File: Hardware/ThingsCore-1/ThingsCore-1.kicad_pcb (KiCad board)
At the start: 6 copper layers, 30 x 51 mm, 8 parts, among them U2 K4B4G1646E-BYMA, U6 LAN8742A, U7 STM32MP133DAE7, U8 W25Q256JVEIQ, U9 TF-PUSH

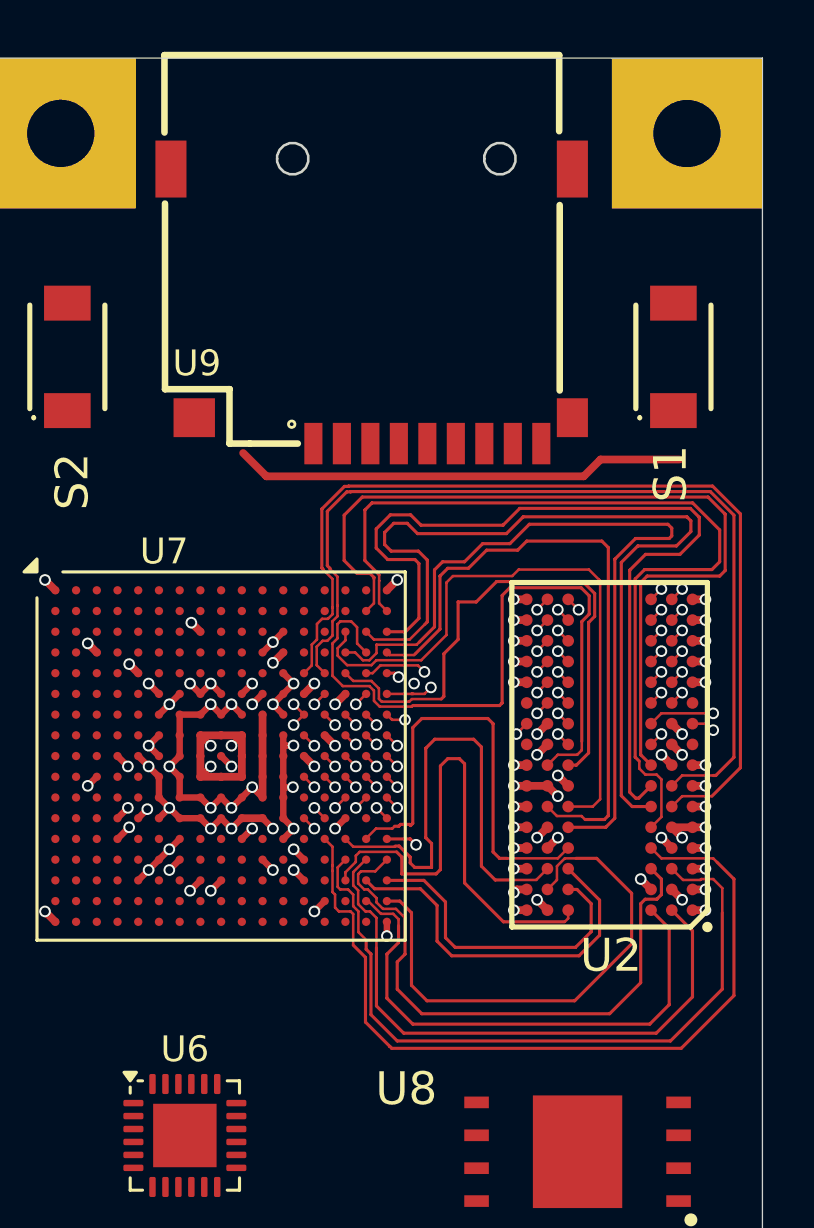
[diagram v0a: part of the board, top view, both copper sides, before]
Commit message: rules and ddr3 reroute
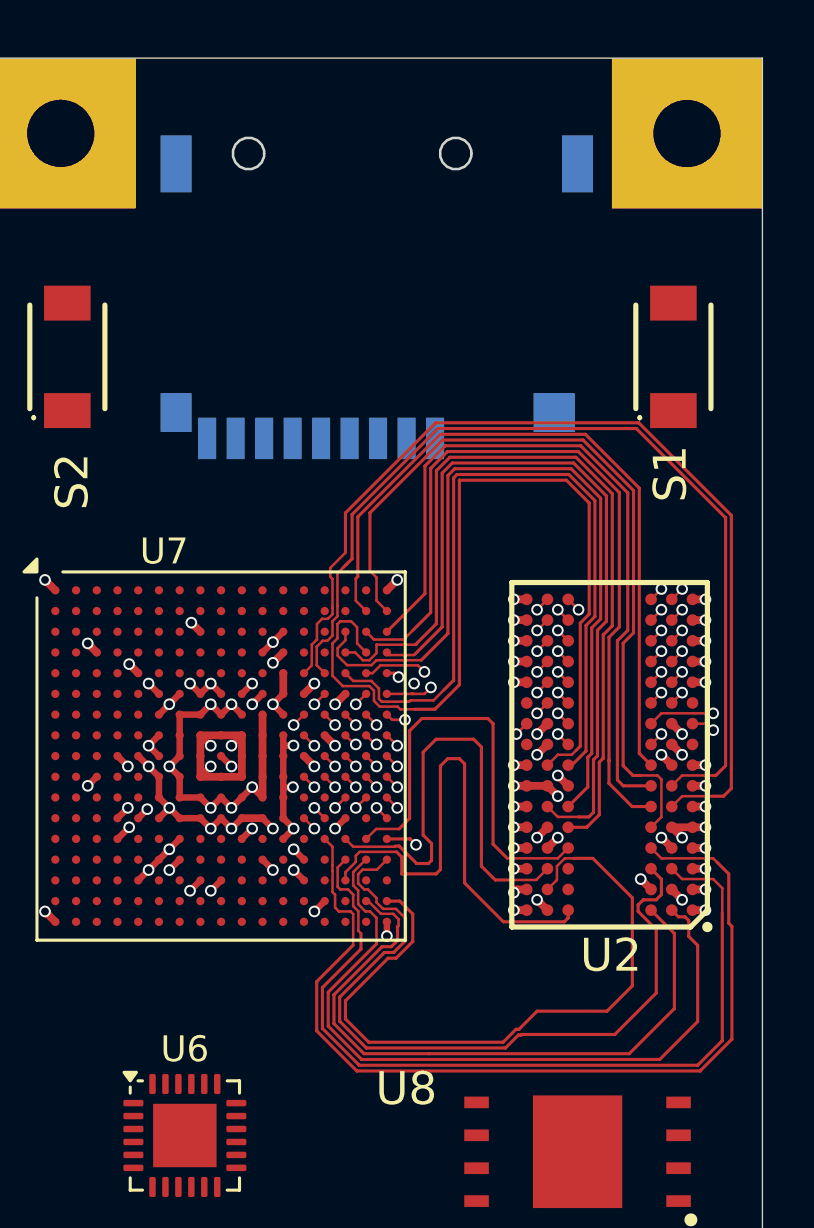
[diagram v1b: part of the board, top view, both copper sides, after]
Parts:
- U9: moved to B.Cu
- moved U9 18.0 mm to (36.4, 28.4), turned to 180 degrees
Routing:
- net /DDR3/DDR_BA2: track 1.54 -> 34.7 mm, vias 3 -> 2
- net /DDR3/DDR_A11: track 1.13 -> 27.6 mm
- net /DDR3/DDR_A13: track 1.13 -> 21.7 mm
- net /DDR3/DDR_A14: track 1.13 -> 18.7 mm
- net (no net): track 17.5 -> 0.00 mm
- net /DDR3/DDR_A12: track 1.13 -> 17.5 mm
- net /DDR3/DDR_DQS1N: track 14.4 -> 0.00 mm
- net /DDR3/DDR_RESETN: track 1.08 -> 15.3 mm
- net /DDR3/DDR_DQS1P: track 12.2 -> 0.00 mm
- net /DDR3/DDR_D7: track 21.5 -> 29.7 mm
- net /DDR3/DDR_D5: track 26.8 -> 34.5 mm
- net /DDR3/DDR_D1: track 24.0 -> 31.0 mm
- net /DDR3/DDR_D14: track 20.2 -> 27.0 mm
- net /DDR3/DDR_D9: track 22.5 -> 28.9 mm
- net /DDR3/DDR_D3: track 24.7 -> 30.1 mm
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
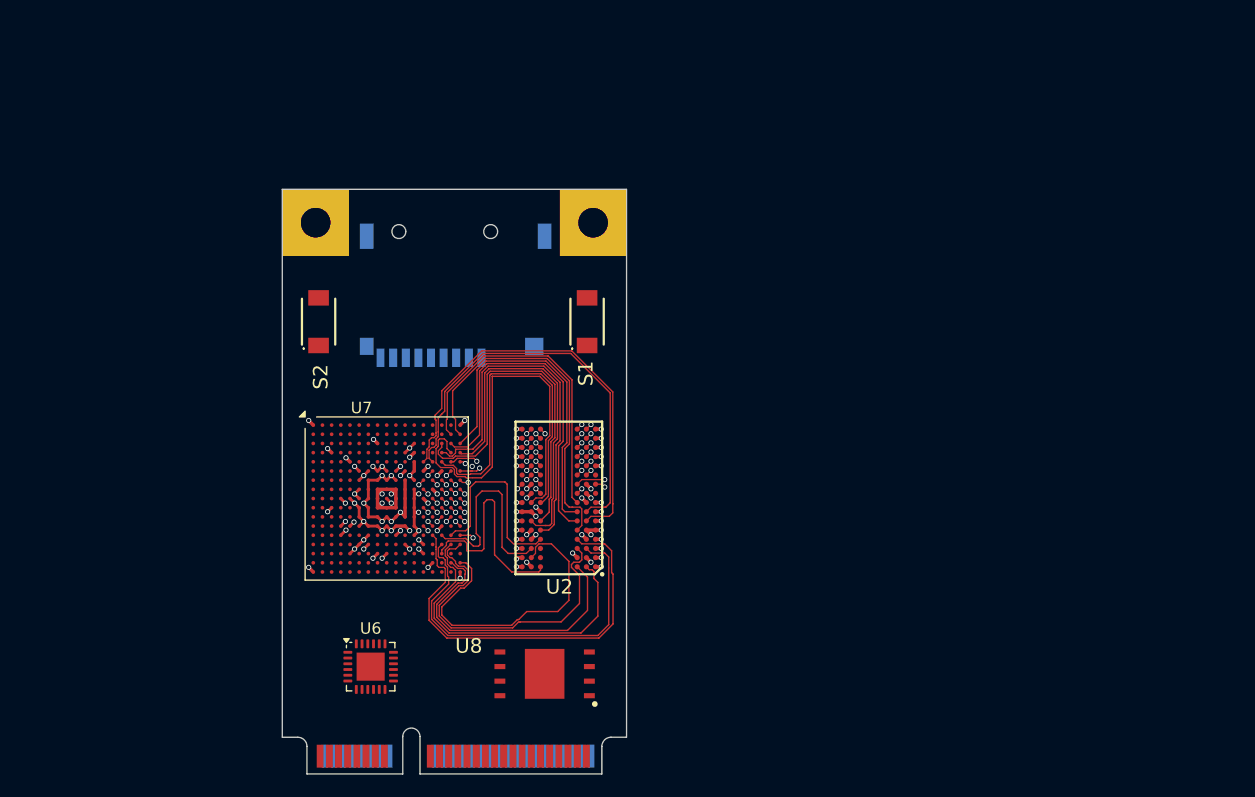
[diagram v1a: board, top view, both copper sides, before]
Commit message: ddr3 fanout done
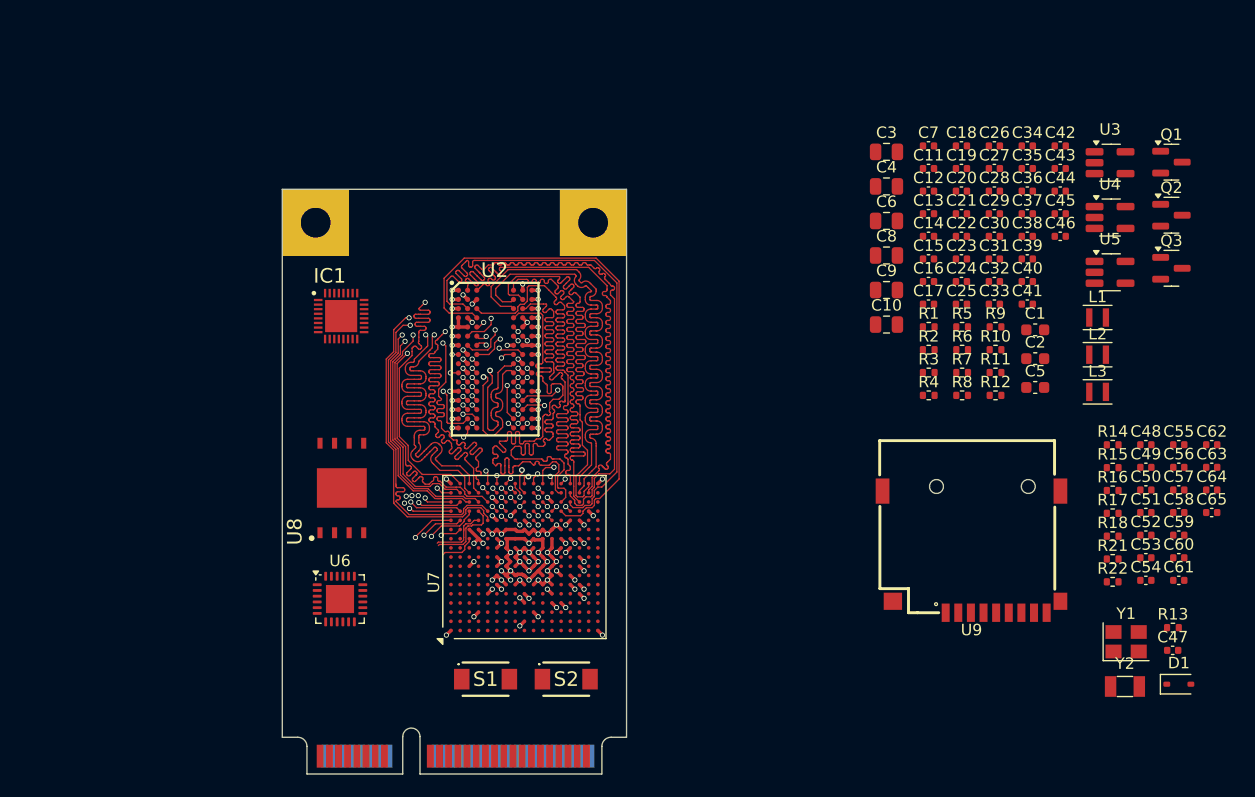
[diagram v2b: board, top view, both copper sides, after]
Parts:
- added C1: 4.7u, Capacitor_SMD:C_0603_1608Metric, F.Cu at (78.0, 24.6)
- added C10: 22u, Capacitor_SMD:C_0805_2012Metric, F.Cu at (65.1, 24.2)
- added C11: 1u, Capacitor_SMD:C_0402_1005Metric, F.Cu at (68.7, 10.6)
- added C12: 1u, Capacitor_SMD:C_0402_1005Metric, F.Cu at (68.7, 12.6)
- added C13: 1u, Capacitor_SMD:C_0402_1005Metric, F.Cu at (68.7, 14.5)
- added C14: 1n, Capacitor_SMD:C_0402_1005Metric, F.Cu at (68.7, 16.5)
- added C15: 1n, Capacitor_SMD:C_0402_1005Metric, F.Cu at (68.7, 18.5)
- added C16: 1n, Capacitor_SMD:C_0402_1005Metric, F.Cu at (68.7, 20.4)
- added C17: 1n, Capacitor_SMD:C_0402_1005Metric, F.Cu at (68.7, 22.4)
- added C18: 1n, Capacitor_SMD:C_0402_1005Metric, F.Cu at (71.6, 8.62)
- added C19: 1n, Capacitor_SMD:C_0402_1005Metric, F.Cu at (71.6, 10.6)
- added C2: 4.7u, Capacitor_SMD:C_0603_1608Metric, F.Cu at (78.0, 27.2)
- added C20: 1u, Capacitor_SMD:C_0402_1005Metric, F.Cu at (71.6, 12.6)
- added C21: 1u, Capacitor_SMD:C_0402_1005Metric, F.Cu at (71.6, 14.5)
- added C22: 1u, Capacitor_SMD:C_0402_1005Metric, F.Cu at (71.6, 16.5)
- added C23: 1u, Capacitor_SMD:C_0402_1005Metric, F.Cu at (71.6, 18.5)
- added C24: 1u, Capacitor_SMD:C_0402_1005Metric, F.Cu at (71.6, 20.4)
- added C25: 1u, Capacitor_SMD:C_0402_1005Metric, F.Cu at (71.6, 22.4)
- added C26: 1u, Capacitor_SMD:C_0402_1005Metric, F.Cu at (74.5, 8.62)
- added C27: 1u, Capacitor_SMD:C_0402_1005Metric, F.Cu at (74.5, 10.6)
- added C28: 1u, Capacitor_SMD:C_0402_1005Metric, F.Cu at (74.5, 12.6)
- added C29: 1u, Capacitor_SMD:C_0402_1005Metric, F.Cu at (74.5, 14.5)
- added C3: 22u, Capacitor_SMD:C_0805_2012Metric, F.Cu at (65.1, 9.14)
- added C30: 1u, Capacitor_SMD:C_0402_1005Metric, F.Cu at (74.5, 16.5)
- added C31: 1u, Capacitor_SMD:C_0402_1005Metric, F.Cu at (74.5, 18.5)
- added C32: 1u, Capacitor_SMD:C_0402_1005Metric, F.Cu at (74.5, 20.4)
- added C33: 1u, Capacitor_SMD:C_0402_1005Metric, F.Cu at (74.5, 22.4)
- added C34: 1u, Capacitor_SMD:C_0402_1005Metric, F.Cu at (77.3, 8.62)
- added C35: 1u, Capacitor_SMD:C_0402_1005Metric, F.Cu at (77.3, 10.6)
- added C36: 1u, Capacitor_SMD:C_0402_1005Metric, F.Cu at (77.3, 12.6)
- added C37: 1u, Capacitor_SMD:C_0402_1005Metric, F.Cu at (77.3, 14.5)
- added C38: 1u, Capacitor_SMD:C_0402_1005Metric, F.Cu at (77.3, 16.5)
- added C39: 1u, Capacitor_SMD:C_0402_1005Metric, F.Cu at (77.3, 18.5)
- added C4: 22u, Capacitor_SMD:C_0805_2012Metric, F.Cu at (65.1, 12.2)
- added C40: 1u, Capacitor_SMD:C_0402_1005Metric, F.Cu at (77.3, 20.4)
- added C41: 2.2u, Capacitor_SMD:C_0402_1005Metric, F.Cu at (77.3, 22.4)
- added C42: 2.2u, Capacitor_SMD:C_0402_1005Metric, F.Cu at (80.2, 8.62)
- added C43: 1u, Capacitor_SMD:C_0402_1005Metric, F.Cu at (80.2, 10.6)
- added C44: 100n, Capacitor_SMD:C_0402_1005Metric, F.Cu at (80.2, 12.6)
- added C45: 1u, Capacitor_SMD:C_0402_1005Metric, F.Cu at (80.2, 14.5)
- added C46: 100n, Capacitor_SMD:C_0402_1005Metric, F.Cu at (80.2, 16.5)
- added C47: 100n, Capacitor_SMD:C_0402_1005Metric, F.Cu at (90.0, 52.6)
- added C48: 100n, Capacitor_SMD:C_0402_1005Metric, F.Cu at (87.7, 34.7)
- added C49: 100n, Capacitor_SMD:C_0402_1005Metric, F.Cu at (87.7, 36.6)
- added C5: 4.7u, Capacitor_SMD:C_0603_1608Metric, F.Cu at (78.0, 29.7)
- added C50: 100n, Capacitor_SMD:C_0402_1005Metric, F.Cu at (87.7, 38.6)
- added C51: 1u, Capacitor_SMD:C_0402_1005Metric, F.Cu at (87.7, 40.6)
- added C52: 1u, Capacitor_SMD:C_0402_1005Metric, F.Cu at (87.7, 42.5)
- added C53: 1u, Capacitor_SMD:C_0402_1005Metric, F.Cu at (87.7, 44.5)
- added C54: 1u, Capacitor_SMD:C_0402_1005Metric, F.Cu at (87.7, 46.5)
- added C55: 1u, Capacitor_SMD:C_0402_1005Metric, F.Cu at (90.5, 34.7)
- added C56: 1u, Capacitor_SMD:C_0402_1005Metric, F.Cu at (90.5, 36.6)
- added C57: 100n, Capacitor_SMD:C_0402_1005Metric, F.Cu at (90.5, 38.6)
- added C58: 100n, Capacitor_SMD:C_0402_1005Metric, F.Cu at (90.5, 40.6)
- added C59: 100n, Capacitor_SMD:C_0402_1005Metric, F.Cu at (90.5, 42.5)
- added C6: 22u, Capacitor_SMD:C_0805_2012Metric, F.Cu at (65.1, 15.2)
- added C60: 100n, Capacitor_SMD:C_0402_1005Metric, F.Cu at (90.5, 44.5)
- added C61: 100n, Capacitor_SMD:C_0402_1005Metric, F.Cu at (90.5, 46.5)
- added C62: 100n, Capacitor_SMD:C_0402_1005Metric, F.Cu at (93.4, 34.7)
- added C63: 100n, Capacitor_SMD:C_0402_1005Metric, F.Cu at (93.4, 36.6)
- added C64: 100n, Capacitor_SMD:C_0402_1005Metric, F.Cu at (93.4, 38.6)
- added C65: 100n, Capacitor_SMD:C_0402_1005Metric, F.Cu at (93.4, 40.6)
- added C7: C, Capacitor_SMD:C_0402_1005Metric, F.Cu at (68.7, 8.62)
- added C8: 22u, Capacitor_SMD:C_0805_2012Metric, F.Cu at (65.1, 18.2)
- added C9: 22u, Capacitor_SMD:C_0805_2012Metric, F.Cu at (65.1, 21.2)
- added D1: 1N4148WS, Diode_SMD:D_SOD-323, F.Cu at (90.5, 55.5)
- added IC1: WF200SD, ThingsCore-1:QFN40P400X400X90-33N-D, F.Cu at (17.5, 23.4)
- added L1: 2.2u, Inductor_SMD:L_Murata_DFE201610P, F.Cu at (83.5, 23.6)
- added L2: 2.2u, Inductor_SMD:L_Murata_DFE201610P, F.Cu at (83.5, 26.8)
- added L3: 2.2u, Inductor_SMD:L_Murata_DFE201610P, F.Cu at (83.5, 30.1)
- added Q1: Si2371EDS, Package_TO_SOT_SMD:SOT-23, F.Cu at (89.9, 10.0)
- added Q2: Si2371EDS, Package_TO_SOT_SMD:SOT-23, F.Cu at (89.9, 14.7)
- added Q3: 2N7002, Package_TO_SOT_SMD:SOT-23, F.Cu at (89.9, 19.3)
- added R1: R, Resistor_SMD:R_0402_1005Metric, F.Cu at (68.7, 24.4)
- added R10: 1k, Resistor_SMD:R_0402_1005Metric, F.Cu at (74.6, 26.4)
- added R11: 10k, Resistor_SMD:R_0402_1005Metric, F.Cu at (74.6, 28.4)
- added R12: 10k, Resistor_SMD:R_0402_1005Metric, F.Cu at (74.6, 30.4)
- added R13: 1k, Resistor_SMD:R_0402_1005Metric, F.Cu at (90.0, 50.6)
- added R14: 100, Resistor_SMD:R_0402_1005Metric, F.Cu at (84.8, 34.7)
- added R15: 240R 1%, Resistor_SMD:R_0402_1005Metric, F.Cu at (84.8, 36.7)
- added R16: 10k, Resistor_SMD:R_0402_1005Metric, F.Cu at (84.8, 38.6)
- added R17: 10k, Resistor_SMD:R_0402_1005Metric, F.Cu at (84.8, 40.6)
- added R18: 240R 1%, Resistor_SMD:R_0402_1005Metric, F.Cu at (84.8, 42.6)
- added R2: R, Resistor_SMD:R_0402_1005Metric, F.Cu at (68.7, 26.4)
- added R21: 1k 1%, Resistor_SMD:R_0402_1005Metric, F.Cu at (84.8, 44.6)
- added R22: 1k 1%, Resistor_SMD:R_0402_1005Metric, F.Cu at (84.8, 46.6)
- added R3: R, Resistor_SMD:R_0402_1005Metric, F.Cu at (68.7, 28.4)
- added R4: R, Resistor_SMD:R_0402_1005Metric, F.Cu at (68.7, 30.4)
- added R5: R, Resistor_SMD:R_0402_1005Metric, F.Cu at (71.6, 24.4)
- added R6: R, Resistor_SMD:R_0402_1005Metric, F.Cu at (71.6, 26.4)
- added R7: R, Resistor_SMD:R_0402_1005Metric, F.Cu at (71.6, 28.4)
- added R8: R, Resistor_SMD:R_0402_1005Metric, F.Cu at (71.6, 30.4)
- added R9: 0R, Resistor_SMD:R_0402_1005Metric, F.Cu at (74.6, 24.4)
- added U3: TLV62569DBV, Package_TO_SOT_SMD:SOT-23-5_HandSoldering, F.Cu at (84.5, 10.1)
- added U4: TLV62569DBV, Package_TO_SOT_SMD:SOT-23-5_HandSoldering, F.Cu at (84.5, 14.9)
- added U5: TLV62569DBV, Package_TO_SOT_SMD:SOT-23-5_HandSoldering, F.Cu at (84.5, 19.6)
- added Y1: X322516MLB4SI, Crystal:Crystal_SMD_3225-4Pin_3.2x2.5mm, F.Cu at (85.9, 51.8)
- added Y2: Q13FC13500004, Crystal:Crystal_SMD_3215-2Pin_3.2x1.5mm, F.Cu at (85.8, 55.7)
- U9: moved to F.Cu
- moved S2 37.9 mm to (37.1, 55.1), turned to 0 degrees
- moved U9 35.1 mm to (63.6, 50.6), turned to 0 degrees
- moved S1 32.4 mm to (30.1, 55.1), turned to 0 degrees
- moved U8 24.0 mm to (17.6, 38.4), turned to 90 degrees
- moved U2 13.3 mm to (30.9, 27.2), turned to 0 degrees
- moved U7 13.0 mm to (33.5, 44.5), turned to 90 degrees
- moved U6 6.47 mm to (17.4, 48.1)
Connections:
- U7 pad J16: /DDR3/DDR_CLK_P -> /DDR3/DDR_CLK_N
- U7 pad J17: /DDR3/DDR_CLK_N -> /DDR3/DDR_CLK_P
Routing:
- net /DDR3/DDR_DQS1N: track 0.00 -> 46.6 mm
- net /DDR3/DDR_RASN: track 1.06 -> 44.8 mm
- net /DDR3/DDR_DQS1P: track 0.00 -> 43.6 mm
- net /DDR3/DDR_A15: track 1.13 -> 43.7 mm
- net /DDR3/DDR_A0: track 1.13 -> 42.8 mm
- net /DDR3/DDR_A3: track 1.13 -> 42.5 mm
- net /DDR3/DDR_CKE: track 1.13 -> 42.2 mm
- net /DDR3/DDR_A7: track 1.13 -> 42.2 mm
- net /DDR3/DDR_WEN: track 1.13 -> 42.1 mm
- net /DDR3/DDR_BA0: track 1.35 -> 42.3 mm
- net /DDR3/DDR_A6: track 1.13 -> 42.0 mm
- net /DDR3/DDR_BA1: track 1.13 -> 41.9 mm
- net /DDR3/DDR_A8: track 1.13 -> 41.7 mm
- net /DDR3/DDR_CLK_N: track 1.13 -> 41.6 mm
- net /DDR3/DDR_A10: track 1.13 -> 41.4 mm
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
